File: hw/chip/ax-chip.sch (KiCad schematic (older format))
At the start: 78 parts, among them IC1 CHIPv1_0, IC2 TPS73433, IC3 AX5043, IC4 TG-5006CJ, J1 CONN_01x02, J2 CONN_01x02, P1 PAD, P2 COAX, P3 COAX, Q1 NX7002AK, U1 DS2401P, U2 MGA-62563, X1 CONN, X2 CONN

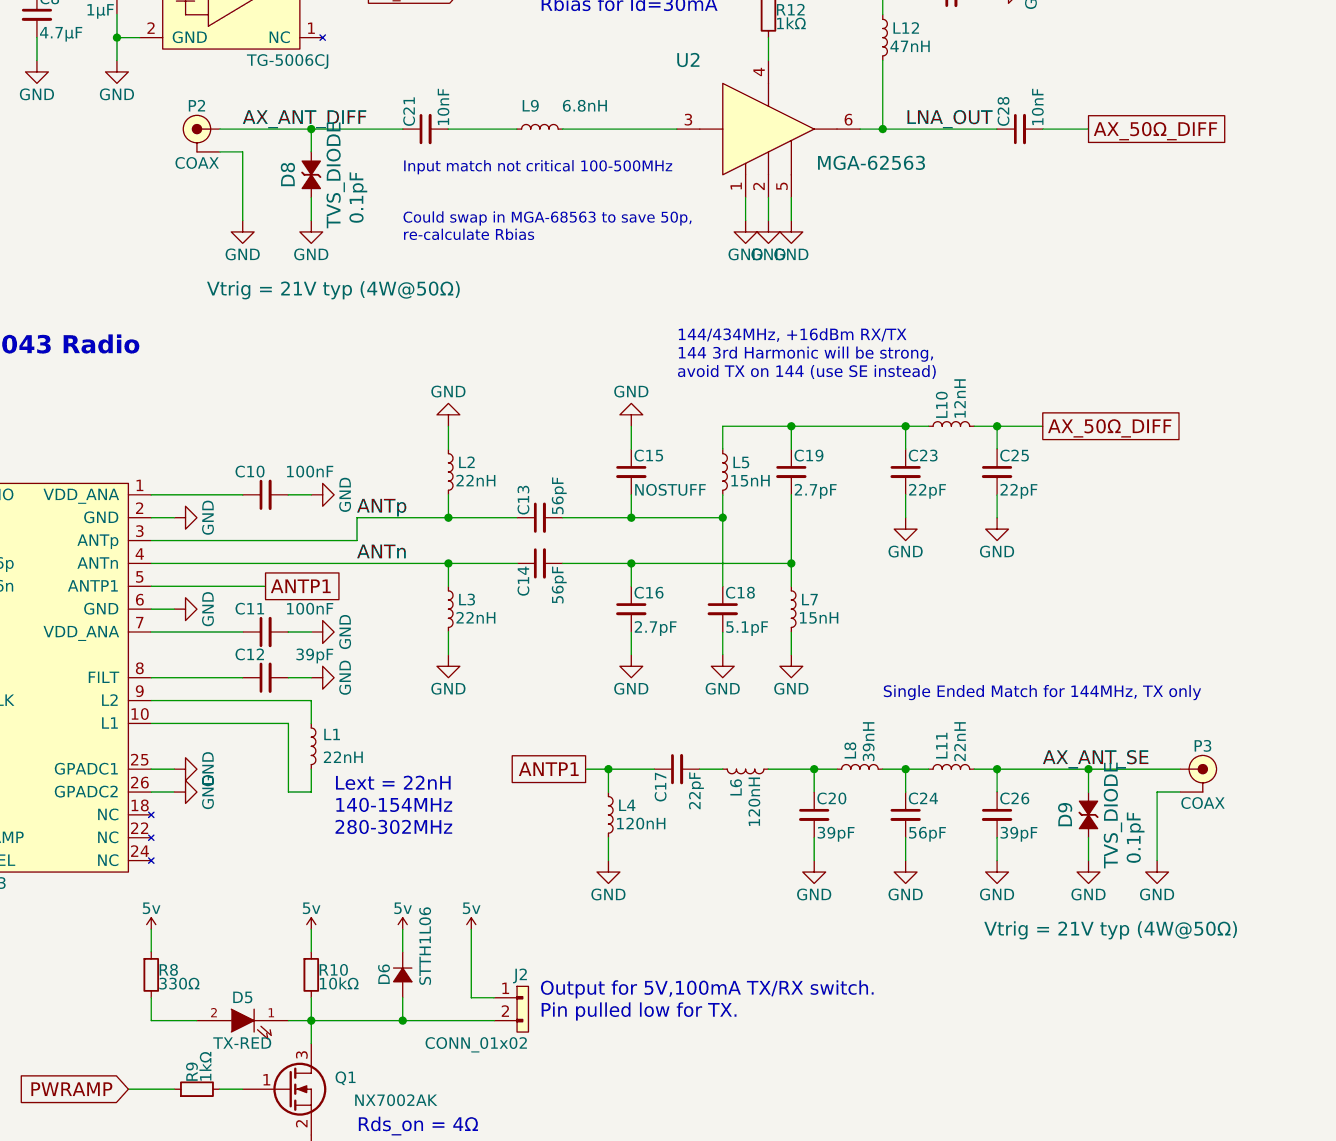
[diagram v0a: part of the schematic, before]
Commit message: [hw] tidy boms, regen artifacts, update READMEs
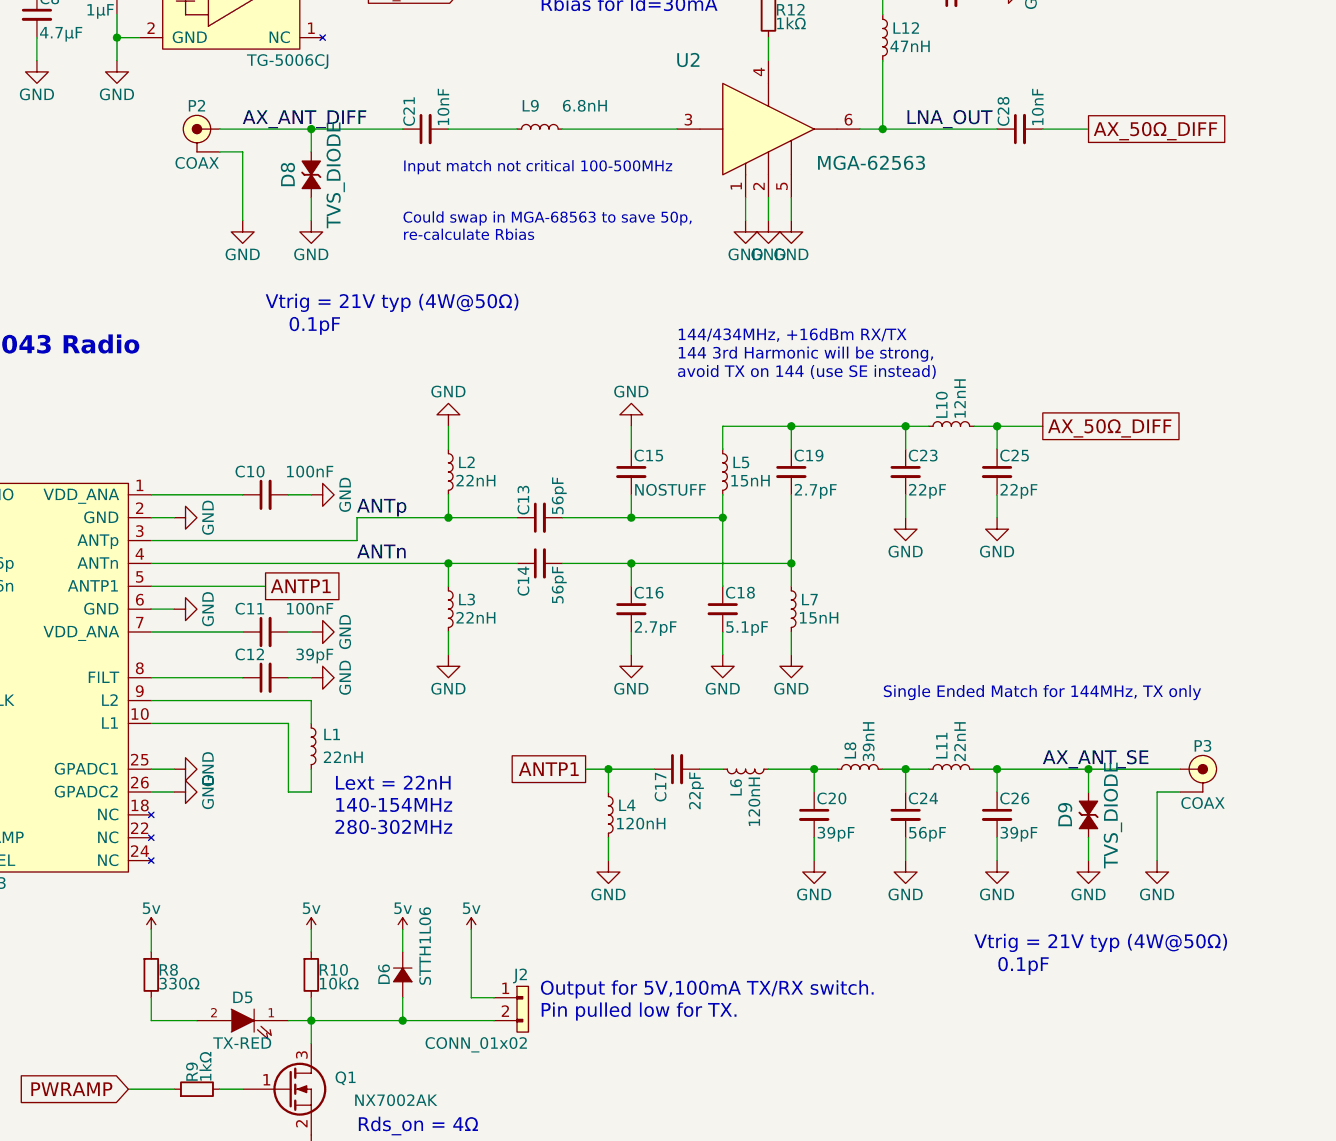
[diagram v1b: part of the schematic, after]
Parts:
- D8, D9: Capacitance 0.1pF -> (none); Vtrig Vtrig = 21V typ (4W@50Ω) -> (none)
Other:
- note added: "0.1pF"
- note added: "Vtrig = 21V typ (4W@50Ω)"
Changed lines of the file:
@@
 LIBS:Vishay
 LIBS:Xilinx
-LIBS:ax-gateway-cache
 LIBS:ax5243
 LIBS:agg-kicad
@@
 F 3 "http://www.farnell.com/datasheets/1992039.pdf" H 7200 2100 60  0001 C CNN
 F 4 "2480929" H 7100 2000 60  0001 C CNN "Farnell"
-F 5 "0.1pF" H 7300 1800 60  0000 C CNN "Capacitance"
-F 6 "Vtrig = 21V typ (4W@50Ω)" V 7700 1900 60  0000 C CNN "Vtrig"
 	1    7100 2000
 	0    -1   1    0
@@
 F 3 "http://www.farnell.com/datasheets/1992039.pdf" H 10600 4900 60  0001 C CNN
 F 4 "2480929" H 10500 4800 60  0001 C CNN "Farnell"
-F 5 "0.1pF" H 10700 4600 60  0000 C CNN "Capacitance"
-F 6 "Vtrig = 21V typ (4W@50Ω)" V 11100 4700 60  0000 C CNN "Vtrig"
 	1    10500 4800
 	0    -1   1    0
@@
 Wire Wire Line
 	10500 1900 10300 1900
+Text Notes 10000 5500 0    60   ~ 0
+Vtrig = 21V typ (4W@50Ω)
+Text Notes 10100 5600 0    60   ~ 0
+0.1pF
+Text Notes 6900 2700 0    60   ~ 0
+Vtrig = 21V typ (4W@50Ω)
+Text Notes 7000 2800 0    60   ~ 0
+0.1pF
 $EndSCHEMATC

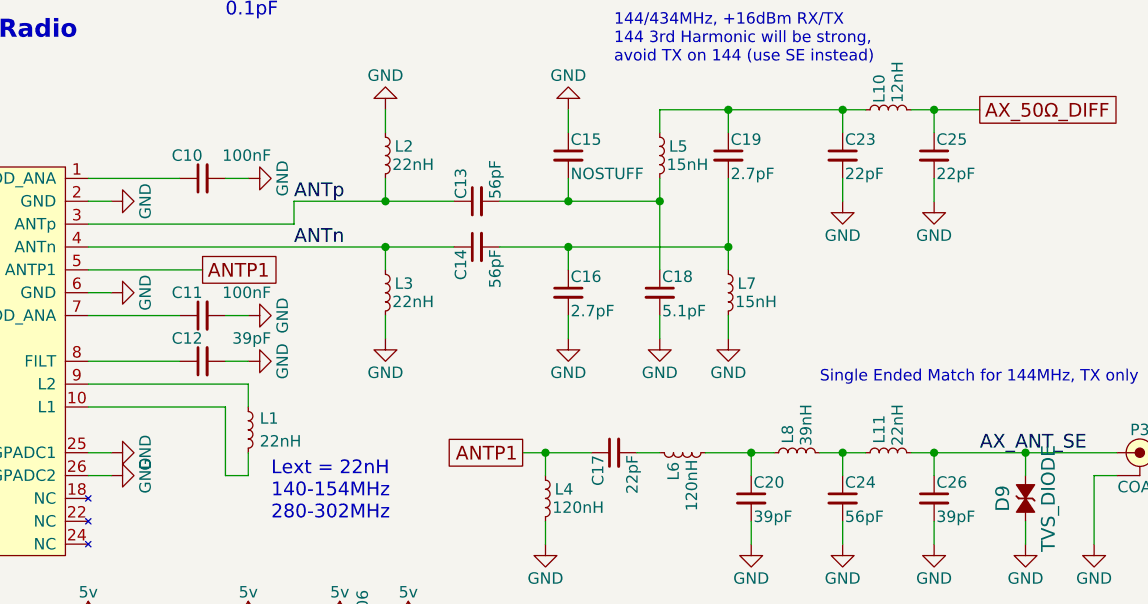
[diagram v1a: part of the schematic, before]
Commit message: [chip] add digikey, farnell order codes
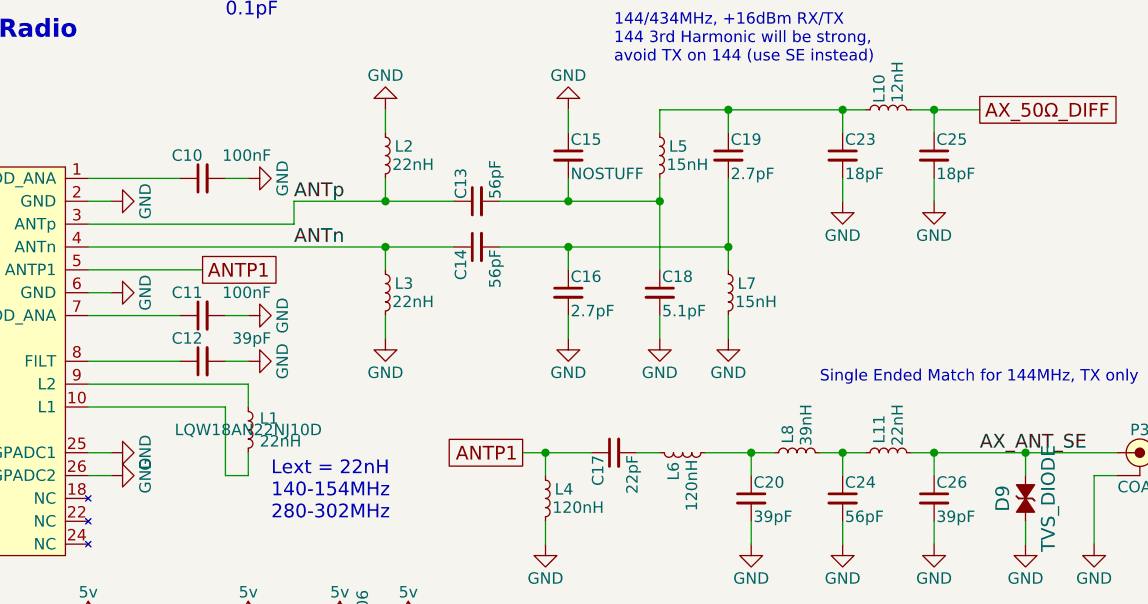
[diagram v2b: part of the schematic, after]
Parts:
- C23, C25: value 22pF -> 18pF; STD.PAS 22pF -> 18pF
- J1, J2: Farnell (none) -> 3882615
- L1, L2, L3: Digikey (none) -> 490-6876-1-ND; STD.PAS 22nH -> (none)
- L4, L6: Digikey (none) -> 490-1180-1-ND; STD.PAS 120nH -> (none)
- L8: Digikey (none) -> 490-2630-1-ND; STD.PAS 39nH -> (none)
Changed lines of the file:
@@
 F 1 "22nH" H 7730 3360 50  0000 L CNN
 F 2 "agg:0603" H 7700 3400 50  0001 C CNN
-F 3 "" H 7700 3400 50  0000 C CNN
-F 4 "22nH" H 7700 3400 60  0001 C CNN "STD.PAS"
+F 3 "LQW18AN22NJ10D" H 7700 3400 50  0001 C CNN
+F 4 "490-6876-1-ND" H 7700 3400 60  0001 C CNN "Digikey"
 	1    7700 3400
 	1    0    0    -1
@@
 F 1 "22nH" H 7730 3960 50  0000 L CNN
 F 2 "agg:0603" H 7700 4000 50  0001 C CNN
-F 3 "" H 7700 4000 50  0000 C CNN
-F 4 "22nH" H 7700 4000 60  0001 C CNN "STD.PAS"
+F 3 "LQW18AN22NJ10D" H 7700 4000 50  0001 C CNN
+F 4 "490-6876-1-ND" H 7700 4000 60  0001 C CNN "Digikey"
 	1    7700 4000
 	1    0    0    -1
@@
 F 1 "22nH" H 7150 4550 50  0000 L CNN
 F 2 "agg:0603" H 7100 4600 50  0001 C CNN
-F 3 "" H 7100 4600 50  0000 C CNN
-F 4 "22nH" H 7100 4600 60  0001 C CNN "STD.PAS"
+F 3 "LQW18AN22NJ10D" H 7100 4600 50  0000 C CNN
+F 4 "490-6876-1-ND" H 7100 4600 60  0001 C CNN "Digikey"
 	1    7100 4600
 	1    0    0    -1
@@
 P 10100 3400
 F 0 "C25" H 10110 3470 50  0000 L CNN
-F 1 "22pF" H 10110 3320 50  0000 L CNN
+F 1 "18pF" H 10110 3320 50  0000 L CNN
 F 2 "agg:0402" H 10100 3400 50  0001 C CNN
 F 3 "" H 10100 3400 50  0000 C CNN
-F 4 "22pF" H 10100 3400 60  0001 C CNN "STD.PAS"
+F 4 "18pF" H 10100 3400 60  0001 C CNN "STD.PAS"
 	1    10100 3400
 	1    0    0    -1
@@
 P 9700 3400
 F 0 "C23" H 9710 3470 50  0000 L CNN
-F 1 "22pF" H 9710 3320 50  0000 L CNN
+F 1 "18pF" H 9710 3320 50  0000 L CNN
 F 2 "agg:0402" H 9700 3400 50  0001 C CNN
 F 3 "" H 9700 3400 50  0000 C CNN
-F 4 "22pF" H 9700 3400 60  0001 C CNN "STD.PAS"
+F 4 "18pF" H 9700 3400 60  0001 C CNN "STD.PAS"
 	1    9700 3400
 	1    0    0    -1
@@
 F 1 "120nH" H 8430 4860 50  0000 L CNN
 F 2 "agg:0603" H 8400 4900 50  0001 C CNN
-F 3 "" H 8400 4900 50  0000 C CNN
-F 4 "120nH" H 8400 4900 60  0001 C CNN "STD.PAS"
+F 3 "LQW18ANR12G00D" H 8400 4900 50  0001 C CNN
+F 4 "490-1180-1-ND" H 8400 4900 60  0001 C CNN "Digikey"
 	1    8400 4900
 	1    0    0    -1
@@
 F 1 "120nH" H 9030 4660 50  0000 L CNN
 F 2 "agg:0603" H 9000 4700 50  0001 C CNN
-F 3 "" H 9000 4700 50  0000 C CNN
-F 4 "120nH" H 9000 4700 60  0001 C CNN "STD.PAS"
+F 3 "LQW18ANR12G00D" H 9000 4700 50  0001 C CNN
+F 4 "490-1180-1-ND" H 9000 4700 60  0001 C CNN "Digikey"
 	1    9000 4700
 	0    -1   1    0
@@
 F 1 "39nH" H 9530 4660 50  0000 L CNN
 F 2 "agg:0402" H 9500 4700 50  0001 C CNN
-F 3 "" H 9500 4700 50  0000 C CNN
-F 4 "39nH" H 9500 4700 60  0001 C CNN "STD.PAS"
+F 3 "LQG15HS39NJ02D" H 9500 4700 50  0001 C CNN
+F 4 "490-2630-1-ND" H 9500 4700 60  0001 C CNN "Digikey"
 	1    9500 4700
 	0    -1   -1   0
@@
 F 2 "Terminal_Blocks:TerminalBlock_Pheonix_PT-3.5mm_2pol" H 800 1800 50  0001 C CNN
 F 3 "" H 800 1800 50  0001 C CNN
+F 4 "3882615" H 800 1800 60  0001 C CNN "Farnell"
 	1    800  1800
 	1    0    0    -1
@@
 F 2 "Terminal_Blocks:TerminalBlock_Pheonix_PT-3.5mm_2pol" H 8000 5700 50  0001 C CNN
 F 3 "" H 8000 5700 50  0001 C CNN
+F 4 "3882615" H 8000 5700 60  0001 C CNN "Farnell"
 	1    8000 5700
 	-1   0    0    -1
